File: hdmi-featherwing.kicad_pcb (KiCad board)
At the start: 2 copper layers, 22.9 x 50.8 mm, 11 parts, among them J1 HDMI_A

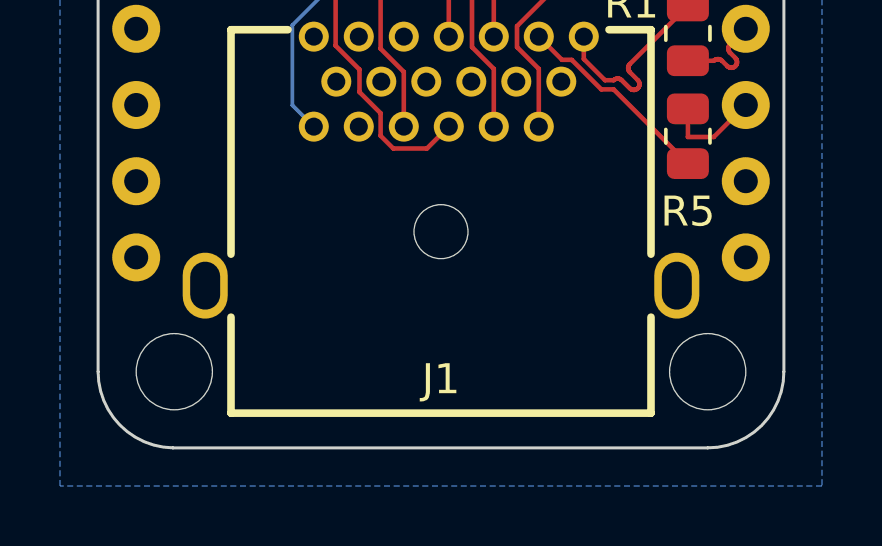
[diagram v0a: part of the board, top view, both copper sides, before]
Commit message: Add JLCJLCJLCJLC silkscreen
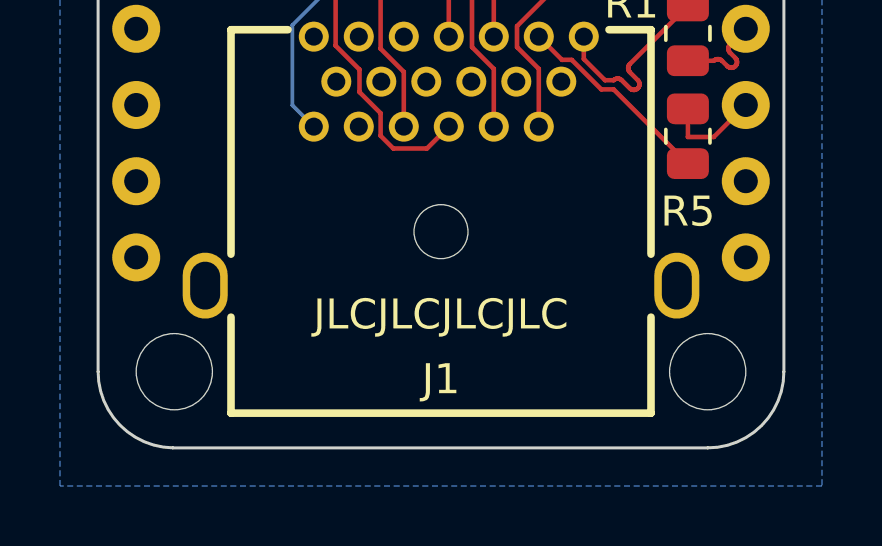
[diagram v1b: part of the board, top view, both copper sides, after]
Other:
- board text added: "JLCJLCJLCJLC"
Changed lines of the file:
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@@
     (pad_to_mask_clearance 0)
     (pcbplotparams
-      (layerselection 0x00010f0_ffffffff)
+      (layerselection 0x00010fc_ffffffff)
       (disableapertmacros false)
       (usegerberextensions false)
@@
       (drillshape 0)
       (scaleselection 1)
-      (outputdirectory "fab/gerbers")
+      (outputdirectory "fab/")
     )
   )
@@
       (effects (font (size 1 1) (thickness 0.15)))
     )
-    (fp_text value "HDMI_A" (at 0 4.9865) (layer "F.Fab")
+    (fp_text value "HDMI_A" (at 0 2.5735 180) (layer "F.Fab")
       (effects (font (size 1.143 1.143) (thickness 0.152)))
     )
@@
     (property "Sheetname" "")
     (property "exclude_from_bom" "")
-    (attr through_hole exclude_from_bom)
+    (attr through_hole exclude_from_pos_files exclude_from_bom)
     (fp_text reference "A1" (at 10.16 -5.499989) (layer "F.SilkS") hide
       (effects (font (size 1 1) (thickness 0.15)))
@@
     (effects (font (size 0.889 0.889) (thickness 0.2032)))
   )
+  (gr_text "JLCJLCJLCJLC" (at 119.38 125.095) (layer "F.SilkS")
+    (effects (font (size 1 1) (thickness 0.15)))
+  )
   (gr_text "*probably not DVI either" (at 119.38 100.965) (layer "F.SilkS")

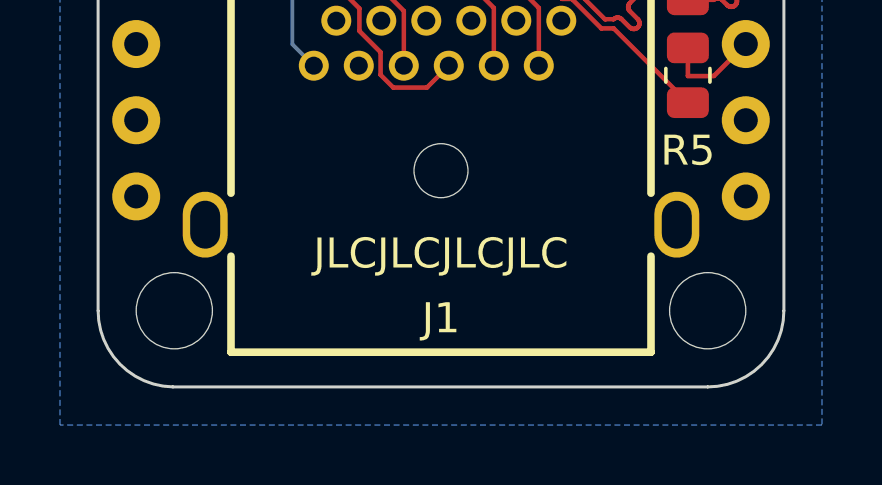
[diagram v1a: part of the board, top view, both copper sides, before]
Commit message: Fix HDMI origin
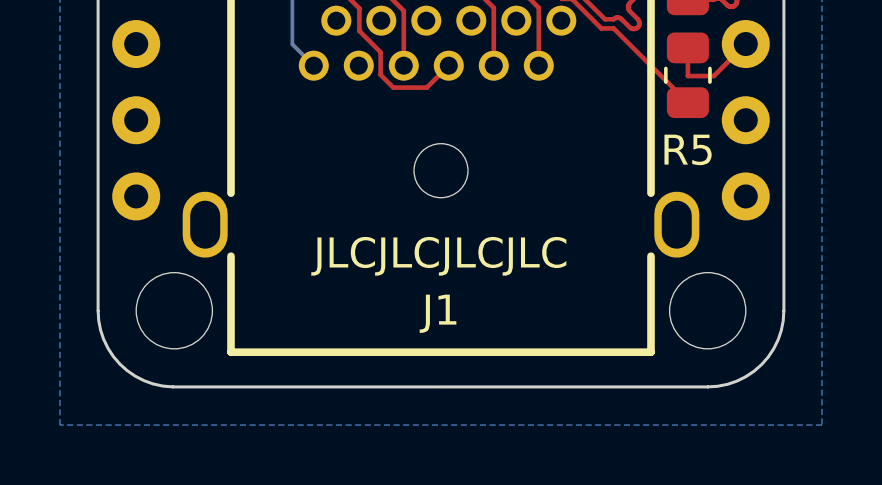
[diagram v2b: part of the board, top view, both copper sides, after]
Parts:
- moved J1 2.01 mm to (119.4, 122.0)
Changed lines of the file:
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@@
   )
   (footprint "HDMI:HDMI-TH_HYC12-HDMIA19-61" (layer "F.Cu")
-    (at 119.38 119.9815)
+    (at 119.38 121.991)
     (property "LCSC" "C711354")
     (property "Sheetfile" "hdmi-featherwing.kicad_sch")
     (property "Sheetname" "")
     (attr through_hole)
-    (fp_text reference "J1" (at 0 7.2725) (layer "F.SilkS")
+    (fp_text reference "J1" (at 0 5.009) (layer "F.SilkS")
       (effects (font (size 1 1) (thickness 0.15)))
     )
-    (fp_text value "HDMI_A" (at 0 2.5735 180) (layer "F.Fab")
+    (fp_text value "HDMI_A" (at 0 -1.341 180) (layer "F.Fab")
       (effects (font (size 1.143 1.143) (thickness 0.152)))
     )
@@
       (effects (font (size 1 1) (thickness 0.15)))
     )
-    (fp_line (start 7 3.1) (end 7 -4.381) (layer "F.SilkS") (width 0.254))
-    (fp_line (start 7 -4.381) (end 5.6 -4.381) (layer "F.SilkS") (width 0.254))
-    (fp_line (start -7 8.4) (end -7 5.2) (layer "F.SilkS") (width 0.254))
-    (fp_line (start -5.1 -4.381) (end -7 -4.381) (layer "F.SilkS") (width 0.254))
-    (fp_line (start 7 8.4) (end 7 5.2) (layer "F.SilkS") (width 0.254))
-    (fp_line (start -7 3.1) (end -7 -4.381) (layer "F.SilkS") (width 0.254))
-    (fp_line (start -7 8.4) (end 7 8.4) (layer "F.SilkS") (width 0.254))
-    (pad "" np_thru_hole circle (at 0 2.35) (locked) (size 1.8 1.8) (drill 1.8) (layers *.Cu *.Mask))
-    (pad "1" thru_hole circle (at 4.76 -4.15) (locked) (size 1 1) (drill 0.6) (layers *.Cu *.Paste *.Mask)
-      (net 41 "/D2+") (pinfunction "D2+") (pintype "passive"))
-    (pad "2" thru_hole circle (at 4.01 -2.65) (locked) (size 1 1) (drill 0.6) (layers *.Cu *.Paste *.Mask)
-      (net 16 "GND") (pinfunction "D2S") (pintype "power_in"))
-    (pad "3" thru_hole circle (at 3.26 -4.15) (locked) (size 1 1) (drill 0.6) (layers *.Cu *.Paste *.Mask)
-      (net 40 "/D2-") (pinfunction "D2-") (pintype "passive"))
-    (pad "4" thru_hole circle (at 3.26 -1.15) (locked) (size 1 1) (drill 0.6) (layers *.Cu *.Paste *.Mask)
-      (net 39 "/D1+") (pinfunction "D1+") (pintype "passive"))
-    (pad "5" thru_hole circle (at 2.51 -2.65) (locked) (size 1 1) (drill 0.6) (layers *.Cu *.Paste *.Mask)
-      (net 16 "GND") (pinfunction "D1S") (pintype "power_in"))
-    (pad "6" thru_hole circle (at 1.76 -1.15) (locked) (size 1 1) (drill 0.6) (layers *.Cu *.Paste *.Mask)
-      (net 38 "/D1-") (pinfunction "D1-") (pintype "passive"))
-    (pad "7" thru_hole circle (at 1.76 -4.15) (locked) (size 1 1) (drill 0.6) (layers *.Cu *.Paste *.Mask)
-      (net 37 "/D0+") (pinfunction "D0+") (pintype "passive"))
-    (pad "8" thru_hole circle (at 1.01 -2.65) (locked) (size 1 1) (drill 0.6) (layers *.Cu *.Paste *.Mask)
-      (net 16 "GND") (pinfunction "D0S") (pintype "power_in"))
-    (pad "9" thru_hole circle (at 0.26 -4.15) (locked) (size 1 1) (drill 0.6) (layers *.Cu *.Paste *.Mask)
-      (net 36 "/D0-") (pinfunction "D0-") (pintype "passive"))
-    (pad "10" thru_hole circle (at 0.26 -1.15) (locked) (size 1 1) (drill 0.6) (layers *.Cu *.Paste *.Mask)
-      (net 35 "/CK+") (pinfunction "CK+") (pintype "passive"))
-    (pad "11" thru_hole circle (at -0.49 -2.65) (locked) (size 1 1) (drill 0.6) (layers *.Cu *.Paste *.Mask)
-      (net 16 "GND") (pinfunction "CKS") (pintype "power_in"))
-    (pad "12" thru_hole circle (at -1.24 -1.15) (locked) (size 1 1) (drill 0.6) (layers *.Cu *.Paste *.Mask)
-      (net 34 "/CK-") (pinfunction "CK-") (pintype "passive"))
-    (pad "13" thru_hole circle (at -1.24 -4.15) (locked) (size 1 1) (drill 0.6) (layers *.Cu *.Paste *.Mask)
-      (net 33 "unconnected-(J1-Pad13)") (pinfunction "CEC") (pintype "bidirectional+no_connect"))
-    (pad "14" thru_hole circle (at -1.99 -2.65) (locked) (size 1 1) (drill 0.6) (layers *.Cu *.Paste *.Mask)
-      (net 32 "unconnected-(J1-Pad14)") (pinfunction "UTILITY") (pintype "passive+no_connect"))
-    (pad "15" thru_hole circle (at -2.74 -4.15) (locked) (size 1 1) (drill 0.6) (layers *.Cu *.Paste *.Mask)
-      (net 31 "unconnected-(J1-Pad15)") (pinfunction "SCL") (pintype "passive+no_connect"))
-    (pad "16" thru_hole circle (at -2.74 -1.15) (locked) (size 1 1) (drill 0.6) (layers *.Cu *.Paste *.Mask)
-      (net 30 "unconnected-(J1-Pad16)") (pinfunction "SDA") (pintype "bidirectional+no_connect"))
-    (pad "17" thru_hole circle (at -3.49 -2.65) (locked) (size 1 1) (drill 0.6) (layers *.Cu *.Paste *.Mask)
-      (net 16 "GND") (pinfunction "GND") (pintype "power_in"))
-    (pad "18" thru_hole circle (at -4.24 -1.15) (locked) (size 1 1) (drill 0.6) (layers *.Cu *.Paste *.Mask)
-      (net 10 "+5V") (pinfunction "+5V") (pintype "power_in"))
-    (pad "19" thru_hole circle (at -4.24 -4.15) (locked) (size 1 1) (drill 0.6) (layers *.Cu *.Paste *.Mask)
-      (net 29 "unconnected-(J1-Pad19)") (pinfunction "HPD") (pintype "passive+no_connect"))
-    (pad "SH" thru_hole oval (at -7.86 4.15) (locked) (size 1.5 2.2) (drill oval 1 1.6) (layers *.Cu *.Paste *.Mask)
-      (net 16 "GND") (pinfunction "SH") (pintype "passive"))
-    (pad "SH" thru_hole oval (at 7.86 4.15) (locked) (size 1.5 2.2) (drill oval 1 1.6) (layers *.Cu *.Paste *.Mask)
-      (net 16 "GND") (pinfunction "SH") (pintype "passive"))
+    (fp_line (start -7 6.3905) (end -7 3.1905) (layer "F.SilkS") (width 0.254))
+    (fp_line (start 7 6.3905) (end 7 3.1905) (layer "F.SilkS") (width 0.254))
+    (fp_line (start 7 -6.3905) (end 5.6 -6.3905) (layer "F.SilkS") (width 0.254))
+    (fp_line (start -7 1.0905) (end -7 -6.3905) (layer "F.SilkS") (width 0.254))
+    (fp_line (start -7 6.3905) (end 7 6.3905) (layer "F.SilkS") (width 0.254))
+    (fp_line (start -5.1 -6.3905) (end -7 -6.3905) (layer "F.SilkS") (width 0.254))
+    (fp_line (start 7 1.0905) (end 7 -6.3905) (layer "F.SilkS") (width 0.254))
+    (pad "" np_thru_hole circle (at 0 0.3405) (locked) (size 1.8 1.8) (drill 1.8) (layers *.Cu *.Mask))
+    (pad "1" thru_hole circle (at 4.76 -6.1595) (locked) (size 1 1) (drill 0.6) (layers *.Cu *.Paste *.Mask)
+      (net 41 "/D2+") (pinfunction "D2+"))
+    (pad "2" thru_hole circle (at 4.01 -4.6595) (locked) (size 1 1) (drill 0.6) (layers *.Cu *.Paste *.Mask)
+      (net 16 "GND") (pinfunction "D2S"))
+    (pad "3" thru_hole circle (at 3.26 -6.1595) (locked) (size 1 1) (drill 0.6) (layers *.Cu *.Paste *.Mask)
+      (net 40 "/D2-") (pinfunction "D2-"))
+    (pad "4" thru_hole circle (at 3.26 -3.1595) (locked) (size 1 1) (drill 0.6) (layers *.Cu *.Paste *.Mask)
+      (net 39 "/D1+") (pinfunction "D1+"))
+    (pad "5" thru_hole circle (at 2.51 -4.6595) (locked) (size 1 1) (drill 0.6) (layers *.Cu *.Paste *.Mask)
+      (net 16 "GND") (pinfunction "D1S"))
+    (pad "6" thru_hole circle (at 1.76 -3.1595) (locked) (size 1 1) (drill 0.6) (layers *.Cu *.Paste *.Mask)
+      (net 38 "/D1-") (pinfunction "D1-"))
+    (pad "7" thru_hole circle (at 1.76 -6.1595) (locked) (size 1 1) (drill 0.6) (layers *.Cu *.Paste *.Mask)
+      (net 37 "/D0+") (pinfunction "D0+"))
+    (pad "8" thru_hole circle (at 1.01 -4.6595) (locked) (size 1 1) (drill 0.6) (layers *.Cu *.Paste *.Mask)
+      (net 16 "GND") (pinfunction "D0S"))
+    (pad "9" thru_hole circle (at 0.26 -6.1595) (locked) (size 1 1) (drill 0.6) (layers *.Cu *.Paste *.Mask)
+      (net 36 "/D0-") (pinfunction "D0-"))
+    (pad "10" thru_hole circle (at 0.26 -3.1595) (locked) (size 1 1) (drill 0.6) (layers *.Cu *.Paste *.Mask)
+      (net 35 "/CK+") (pinfunction "CK+"))
+    (pad "11" thru_hole circle (at -0.49 -4.6595) (locked) (size 1 1) (drill 0.6) (layers *.Cu *.Paste *.Mask)
+      (net 16 "GND") (pinfunction "CKS"))
+    (pad "12" thru_hole circle (at -1.24 -3.1595) (locked) (size 1 1) (drill 0.6) (layers *.Cu *.Paste *.Mask)
+      (net 34 "/CK-") (pinfunction "CK-"))
+    (pad "13" thru_hole circle (at -1.24 -6.1595) (locked) (size 1 1) (drill 0.6) (layers *.Cu *.Paste *.Mask)
+      (net 33 "unconnected-(J1-Pad13)") (pinfunction "CEC"))
+    (pad "14" thru_hole circle (at -1.99 -4.6595) (locked) (size 1 1) (drill 0.6) (layers *.Cu *.Paste *.Mask)
+      (net 32 "unconnected-(J1-Pad14)") (pinfunction "UTILITY"))
+    (pad "15" thru_hole circle (at -2.74 -6.1595) (locked) (size 1 1) (drill 0.6) (layers *.Cu *.Paste *.Mask)
+      (net 31 "unconnected-(J1-Pad15)") (pinfunction "SCL"))
+    (pad "16" thru_hole circle (at -2.74 -3.1595) (locked) (size 1 1) (drill 0.6) (layers *.Cu *.Paste *.Mask)
+      (net 30 "unconnected-(J1-Pad16)") (pinfunction "SDA"))
+    (pad "17" thru_hole circle (at -3.49 -4.6595) (locked) (size 1 1) (drill 0.6) (layers *.Cu *.Paste *.Mask)
+      (net 16 "GND") (pinfunction "GND"))
+    (pad "18" thru_hole circle (at -4.24 -3.1595) (locked) (size 1 1) (drill 0.6) (layers *.Cu *.Paste *.Mask)
+      (net 10 "+5V") (pinfunction "+5V"))
+    (pad "19" thru_hole circle (at -4.24 -6.1595) (locked) (size 1 1) (drill 0.6) (layers *.Cu *.Paste *.Mask)
+      (net 29 "unconnected-(J1-Pad19)") (pinfunction "HPD"))
+    (pad "SH" thru_hole oval (at -7.86 2.1405) (locked) (size 1.5 2.2) (drill oval 1 1.6) (layers *.Cu *.Paste *.Mask)
+      (net 16 "GND") (pinfunction "SH"))
+    (pad "SH" thru_hole oval (at 7.86 2.1405) (locked) (size 1.5 2.2) (drill oval 1 1.6) (layers *.Cu *.Paste *.Mask)
+      (net 16 "GND") (pinfunction "SH"))
   )
   (footprint "Resistor_SMD:R_0805_2012Metric" (layer "F.Cu")

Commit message: clear pcb
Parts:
- removed J1: HDMI_A, HDMI:HDMI-TH_HYC12-HDMIA19-61
- removed R1, R2, R3, R4, R5, R6, R7, R8: 270, Resistor_SMD:R_0805_2012Metric
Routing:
- net +5V: track 25.1 -> 0.00 mm
- net /CK+: track 16.0 -> 0.00 mm
- net /CK-: track 16.0 -> 0.00 mm
- net /D1-: track 12.6 -> 0.00 mm
- net /D1+: track 12.6 -> 0.00 mm
- net /WING_D0+: track 12.1 -> 0.00 mm
- net /WING_D0-: track 12.1 -> 0.00 mm
- net /D2+: track 6.72 -> 0.00 mm
- net /D2-: track 6.72 -> 0.00 mm
- net /WING_D2+: track 3.31 -> 0.00 mm
- net /WING_D2-: track 3.31 -> 0.00 mm
- net /D0+: track 2.78 -> 0.00 mm
- net /D0-: track 2.74 -> 0.00 mm
- net /WING_CK-: track 2.39 -> 0.00 mm
- net /WING_CK+: track 2.39 -> 0.00 mm
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
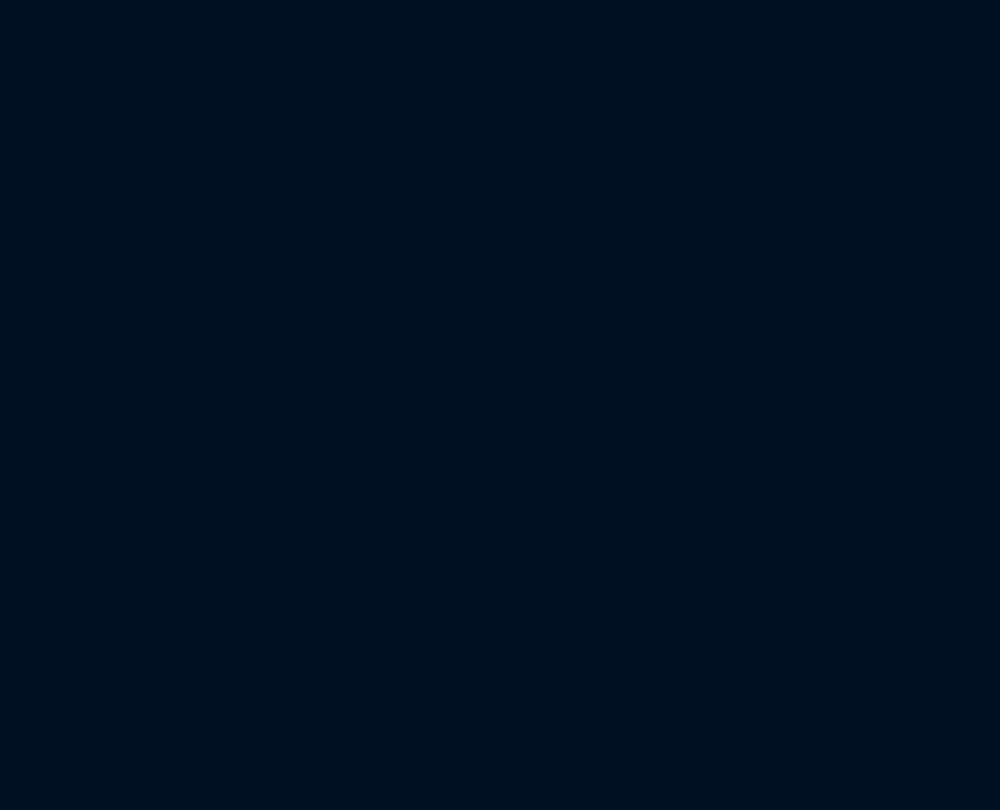
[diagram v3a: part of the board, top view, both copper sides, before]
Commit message: add footprints to pcb
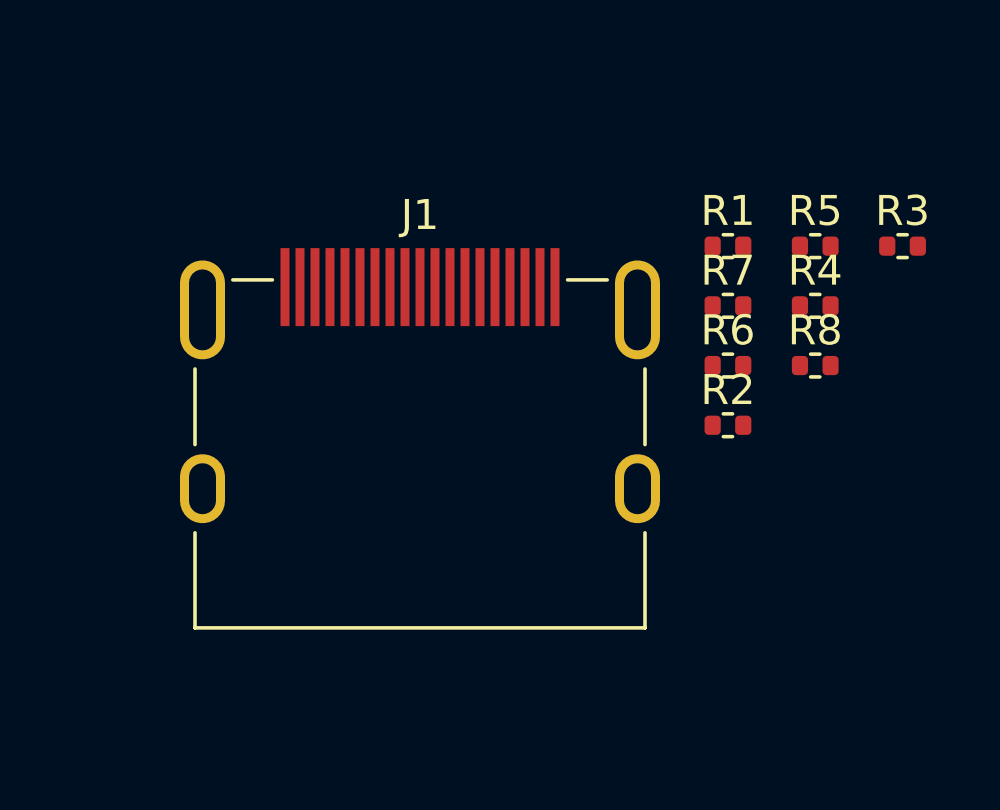
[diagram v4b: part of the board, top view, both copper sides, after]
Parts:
- added J1: HDMI_A, HDMI:KH-HDMI-19P-Cu, F.Cu at (148.0, 99.1)
- added R1: 270, Resistor_SMD:R_0402_1005Metric, F.Cu at (158.2, 94.0)
- added R2: 270, Resistor_SMD:R_0402_1005Metric, F.Cu at (158.2, 99.9)
- added R3: 270, Resistor_SMD:R_0402_1005Metric, F.Cu at (164.0, 94.0)
- added R4: 270, Resistor_SMD:R_0402_1005Metric, F.Cu at (161.1, 95.9)
- added R5: 270, Resistor_SMD:R_0402_1005Metric, F.Cu at (161.1, 94.0)
- added R6: 270, Resistor_SMD:R_0402_1005Metric, F.Cu at (158.2, 97.9)
- added R7: 270, Resistor_SMD:R_0402_1005Metric, F.Cu at (158.2, 95.9)
- added R8: 270, Resistor_SMD:R_0402_1005Metric, F.Cu at (161.1, 97.9)

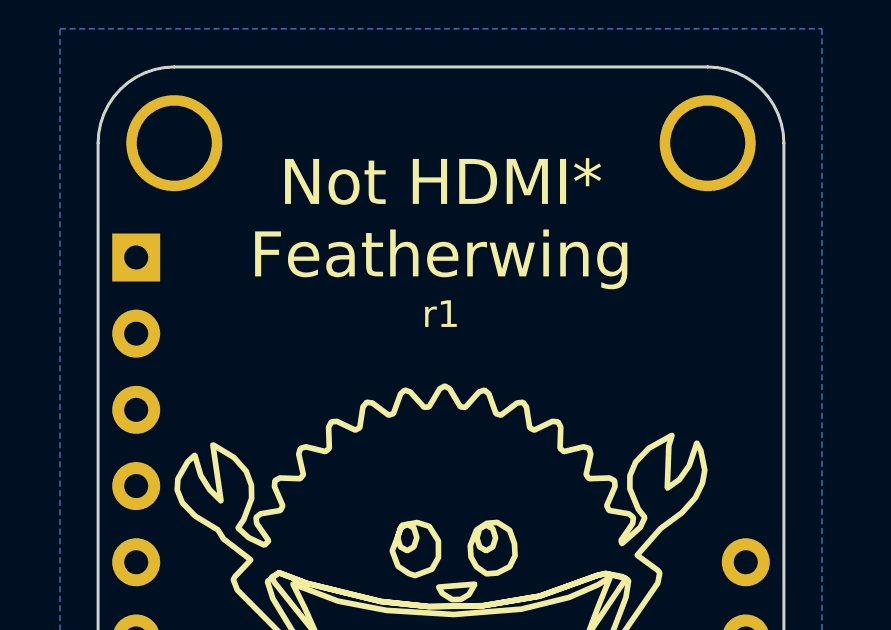
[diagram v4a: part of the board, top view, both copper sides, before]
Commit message: update silkscreen for r2
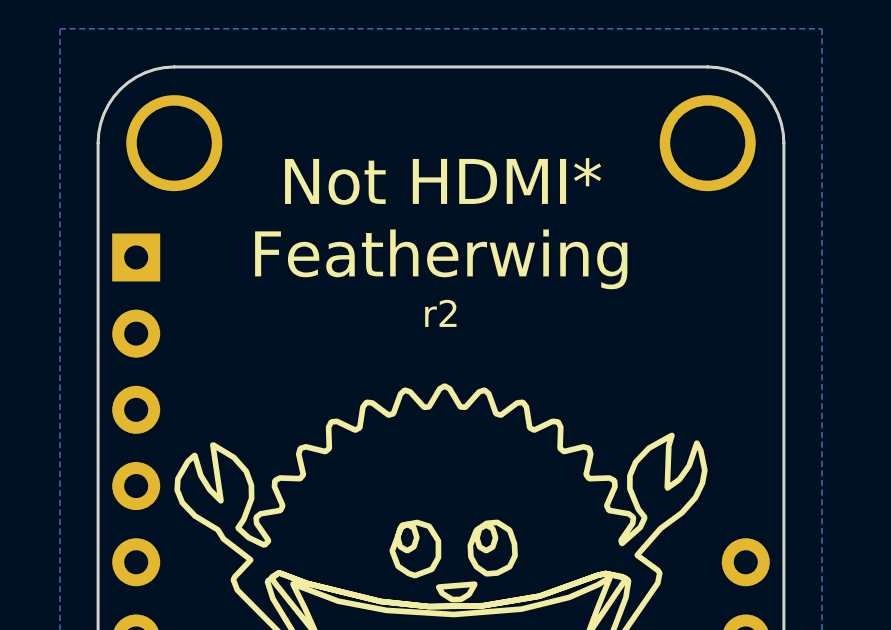
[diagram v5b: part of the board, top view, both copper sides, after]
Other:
- board text added: "r2"
- board text removed: "r1"
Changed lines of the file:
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@@
     (effects (font (size 1.5 1.5) (thickness 0.3)))
   )
-  (gr_text "r1" (at 119.38 86.995) (layer "F.SilkS")
+  (gr_text "r2" (at 119.38 86.995) (layer "F.SilkS")
     (effects (font (size 0.889 0.889) (thickness 0.2032)))
   )
